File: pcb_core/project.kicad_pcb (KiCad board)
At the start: 2 copper layers, 212.3 x 91.7 mm, 143 parts, among them IC1 DRV8871DDA, IC10 DRV8871DDA, IC11 DRV8871DDA, IC12 DRV8871DDA, IC13 DRV8871DDA, IC14 DRV8871DDA, IC15 DRV8871DDA, IC16 DRV8871DDA, IC17 DRV8871DDA, IC18 DRV8871DDA, IC19 SX1509QBIULTRT, IC2 SX1509QBIULTRT, IC3 DRV8871DDA, IC4 TCA9548APWR, IC5 DRV8871DDA, IC6 DRV8871DDA, IC7 DRV8871DDA, IC8 DRV8871DDA, IC9 DRV8871DDA, J1 Conn_01x02, J10 1053131103, J11 1053131103, J12 1053131103, J13 1053131103, J14 1053131103, J15 1053131103, J16 1053131103, J17 1053131103, J18 1053131103, J19 Conn_02x02_Counter_Clockwise, J2 1725656, J20 PCBConnector, J21 PCBConnector, J22 PCBConnector, J23 PCBConnector, J25 PCBConnector, J27 PCBConnector, J3 1053131103, J4 1053131103, J5 1053131103, J6 1053131103, J7 1053131103, J8 1053131103, J9 1053131103, Q1 SI9945BDY-T1-GE3, U1 ESP32-S3-WROOM-2, U2 LTC4365TS8, U3 ESP32-DevKitC

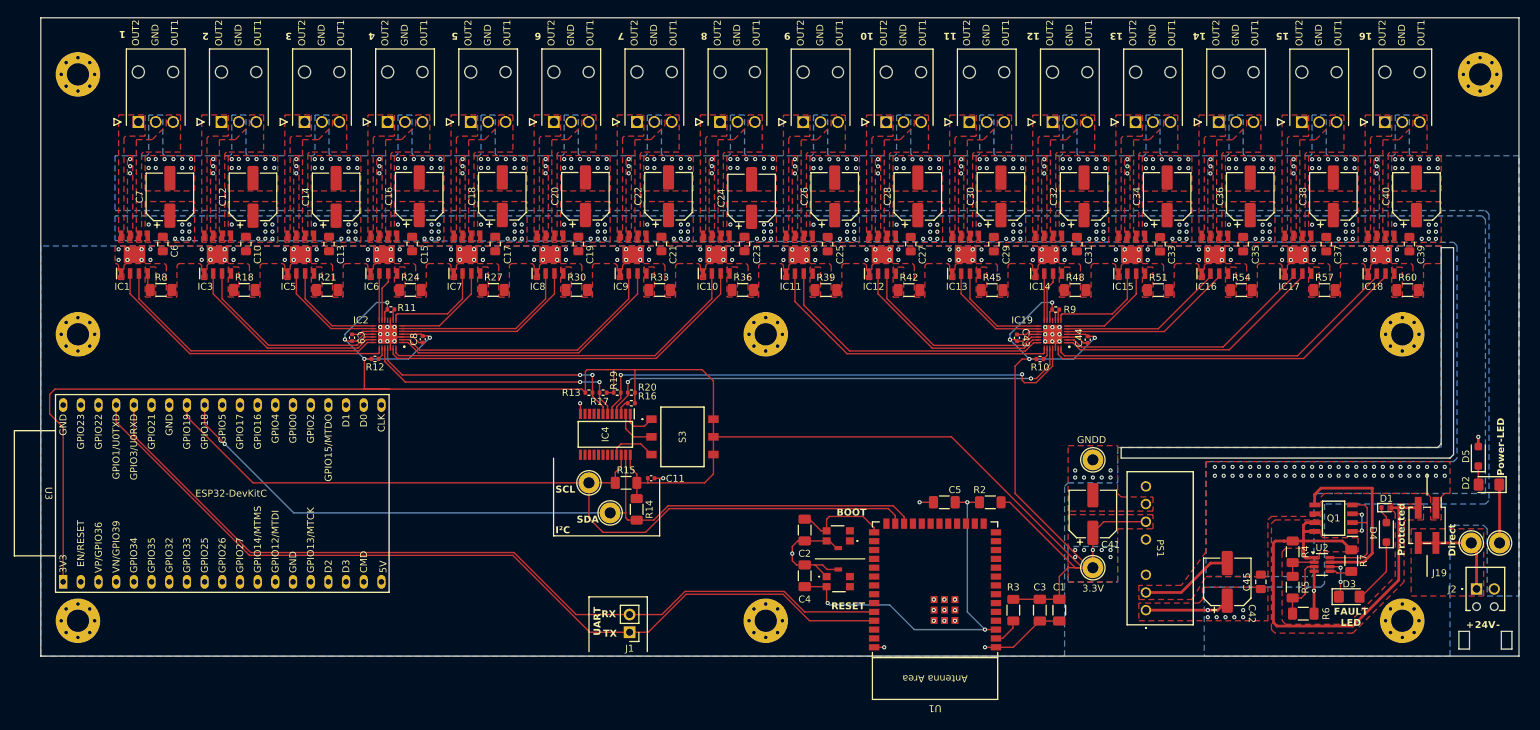
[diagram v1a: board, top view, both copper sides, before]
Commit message: Harmonize package sizing of components
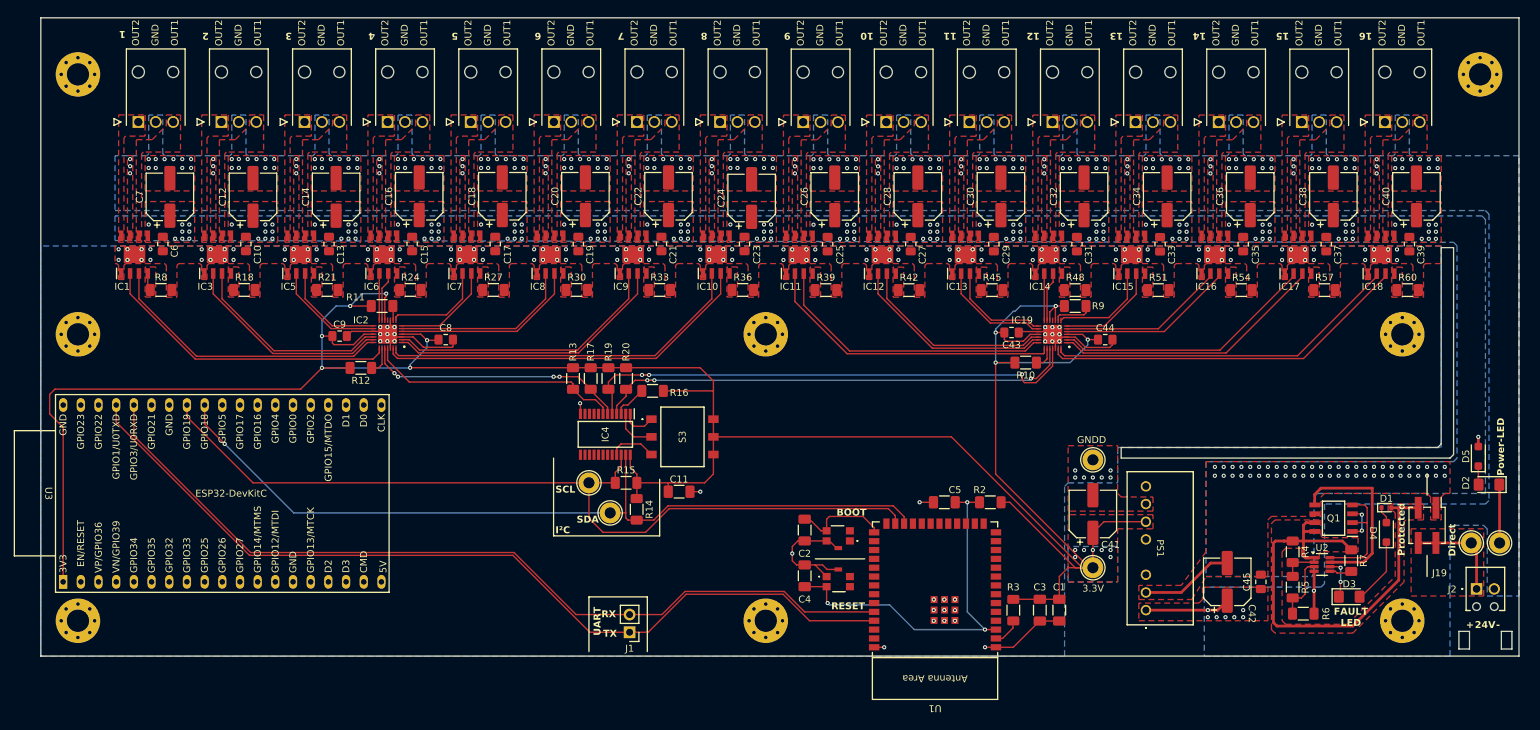
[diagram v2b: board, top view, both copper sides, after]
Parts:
- C11: footprint Capacitor_SMD:C_0402_1005Metric -> Capacitor_SMD:C_1206_3216Metric_Pad1.33x1.80mm_HandSolder
- C43, C44, C8, C9: footprint Capacitor_SMD:C_0402_1005Metric -> Capacitor_SMD:C_0805_2012Metric_Pad1.18x1.45mm_HandSolder
- R10, R11, R12, R13, R16, R17, R19, R20, R9: footprint Resistor_SMD:R_0402_1005Metric -> Resistor_SMD:R_1206_3216Metric_Pad1.30x1.75mm_HandSolder
- moved C11 4.45 mm to (140.0, 109.0)
- moved R16 3.53 mm to (136.1, 94.5)
- moved C8 3.30 mm to (106.4, 87.1), turned to 0 degrees
- moved R13 3.06 mm to (124.7, 92.7), turned to -90 degrees
- moved R9 2.84 mm to (196.8, 82.3)
- moved R17 2.70 mm to (127.3, 92.7), turned to -90 degrees
- moved C44 2.52 mm to (201.2, 87.1), turned to 0 degrees
- moved R12 2.41 mm to (94.2, 91.2)
- moved R19 2.40 mm to (129.8, 92.7), turned to -90 degrees
- moved R20 2.17 mm to (132.3, 92.7), turned to -90 degrees
- moved R10 2.12 mm to (189.7, 90.4)
- moved C9 1.79 mm to (91.2, 86.6), turned to 0 degrees
- moved R11 1.36 mm to (97.3, 82.3)
- moved C43 1.09 mm to (187.7, 86.1), turned to 0 degrees
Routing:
- net VCC_3V3: track 391.6 -> 405.3 mm, vias 15 -> 17
- net GNDD: track 65.7 -> 77.1 mm
- net Net-(IC19-NINT): track 1.63 -> 5.78 mm
- net ~{I2CM_RESET}: track 2.13 -> 4.89 mm
- net Net-(IC2-NRESET): track 1.76 -> 4.05 mm
- net IOEXP01_SCL: track 72.7 -> 74.6 mm, vias 2 -> 3
- net Net-(IC19-NRESET): track 1.76 -> 3.27 mm
- net IOEXP02_SCL: track 38.3 -> 36.9 mm, vias 2 -> 0
- net IN2_2: track 29.7 -> 30.4 mm
- net IN2_1: track 43.0 -> 43.7 mm
- net IN1_1: track 40.9 -> 41.6 mm
- net IN1_2: track 28.7 -> 29.3 mm
- net IOEXP01_SDA: track 69.3 -> 69.8 mm, vias 2 -> 3
- net IOEXP02_SDA: track 39.1 -> 39.4 mm, vias 2 -> 4

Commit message: Update pcb layout
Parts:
- moved C5 17.3 mm to (189.7, 123.2)
- moved R2 16.4 mm to (195.1, 123.2)
- moved R3 7.12 mm to (195.1, 125.7), turned to 180 degrees
- moved C1 4.85 mm to (195.1, 130.8), turned to 180 degrees
- moved C3 4.02 mm to (195.1, 128.3), turned to 180 degrees
- moved D1 0.76 mm to (242.3, 111.3)
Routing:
- net VCC_3V3: track 405.3 -> 367.5 mm
- net /ESP32_EN: track 54.1 -> 42.6 mm, vias 3 -> 2
- net Net-(U1-3V3): track 3.85 -> 9.84 mm
- net GNDA: track 28.9 -> 34.8 mm
- net IOEXP02_SDA: track 39.4 -> 37.9 mm, vias 4 -> 2
- net VIN_24V: track 67.9 -> 66.8 mm
- net IOEXP01_SDA: track 69.8 -> 68.8 mm, vias 3 -> 2
- net IOEXP01_SCL: track 74.6 -> 74.4 mm, vias 3 -> 2
- net PROD_24V: vias 183 -> 156
- net /24V: vias 0 -> 2
- added copper zone on B.Cu, net /24V
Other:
- outline, holes or cut-outs redrawn

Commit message: correct R16 value
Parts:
- R16: value 10K -> 10k
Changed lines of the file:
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@@
 			)
 		)
-		(property "LCSC#" ""
+		(property "LCSC#" "C17902"
 			(at 0 0 180)
 			(unlocked yes)
@@
 			)
 		)
-		(property "LCSC#" ""
+		(property "LCSC#" "C2828875"
 			(at 0 0 -90)
 			(unlocked yes)
@@
 			)
 		)
-		(property "LCSC#" ""
+		(property "LCSC#" "C2828875"
 			(at 0 0 -90)
 			(unlocked yes)
@@
 			)
 		)
+		(property "LCSC#" "C110253"
+			(at 0 0 180)
+			(unlocked yes)
+			(layer "F.Fab")
+			(hide yes)
+			(effects
+				(font
+					(size 1 1)
+					(thickness 0.15)
+				)
+			)
+		)
+		(property "Manufacturer_Part_Number" "Capacitor, 0.1uF, 50V, 10%, 1206 SMD"
+			(at 0 0 180)
+			(unlocked yes)
+			(layer "F.Fab")
+			(hide yes)
+			(effects
+				(font
+					(size 1 1)
+					(thickness 0.15)
+				)
+			)
+		)
 		(property ki_fp_filters "C_*")
 		(sheetname "Stammblatt")
@@
 			)
 		)
+		(property "LCSC#" "C1854361"
+			(at 0 0 180)
+			(unlocked yes)
+			(layer "F.Fab")
+			(hide yes)
+			(effects
+				(font
+					(size 1 1)
+					(thickness 0.15)
+				)
+			)
+		)
 		(property ki_fp_filters "C_*")
 		(sheetname "Stammblatt")
@@
 			)
 		)
+		(property "LCSC#" "C5126164"
+			(at 0 0 0)
+			(unlocked yes)
+			(layer "F.Fab")
+			(hide yes)
+			(effects
+				(font
+					(size 1 1)
+					(thickness 0.15)
+				)
+			)
+		)
 		(property ki_fp_filters "R_*")
 		(sheetname "Stammblatt")
@@
 			)
 		)
+		(property "LCSC#" "C110253"
+			(at 0 0 -90)
+			(unlocked yes)
+			(layer "F.Fab")
+			(hide yes)
+			(effects
+				(font
+					(size 1 1)
+					(thickness 0.15)
+				)
+			)
+		)
+		(property "Manufacturer_Part_Number" "Capacitor, 0.1uF, 50V, 10%, 1206 SMD"
+			(at 0 0 -90)
+			(unlocked yes)
+			(layer "F.Fab")
+			(hide yes)
+			(effects
+				(font
+					(size 1 1)
+					(thickness 0.15)
+				)
+			)
+		)
 		(property ki_fp_filters "C_*")
 		(sheetname "Stammblatt")
@@
 			)
 		)
+		(property "LCSC#" "C17990"
+			(at 0 0 -90)
+			(unlocked yes)
+			(layer "F.Fab")
+			(hide yes)
+			(effects
+				(font
+					(size 1 1)
+					(thickness 0.15)
+				)
+			)
+		)
 		(property ki_fp_filters "R_*")
 		(sheetname "Stammblatt")
@@
 			)
 		)
-		(property "LCSC#" ""
+		(property "LCSC#" "C2828875"
 			(at 0 0 -90)
 			(unlocked yes)
@@
 			)
 		)
-		(property "LCSC#" ""
+		(property "LCSC#" "C17902"
 			(at 0 0 0)
 			(unlocked yes)
@@
 			)
 		)
+		(property "LCSC#" "C2828875"
+			(at 0 0 0)
+			(unlocked yes)
+			(layer "F.Fab")
+			(hide yes)
+			(effects
+				(font
+					(size 1 1)
+					(thickness 0.15)
+				)
+			)
+		)
 		(property ki_fp_filters "R_*")
 		(sheetname "Stammblatt")
@@
 			)
 		)
+		(property "LCSC#" "C14860"
+			(at 0 0 0)
+			(unlocked yes)
+			(layer "F.Fab")
+			(hide yes)
+			(effects
+				(font
+					(size 1 1)
+					(thickness 0.15)
+				)
+			)
+		)
 		(property ki_fp_filters "C_*")
 		(sheetname "Stammblatt")
@@
 			)
 		)
+		(property "LCSC#" "C110253"
+			(at 0 0 90)
+			(unlocked yes)
+			(layer "F.Fab")
+			(hide yes)
+			(effects
+				(font
+					(size 1 1)
+					(thickness 0.15)
+				)
+			)
+		)
+		(property "Manufacturer_Part_Number" "Capacitor, 0.1uF, 50V, 10%, 1206 SMD"
+			(at 0 0 90)
+			(unlocked yes)
+			(layer "F.Fab")
+			(hide yes)
+			(effects
+				(font
+					(size 1 1)
+					(thickness 0.15)
+				)
+			)
+		)
 		(property ki_fp_filters "C_*")
 		(sheetname "Stammblatt")
@@
 			)
 		)
-		(property "Value" "10K"
+		(property "Value" "10k"
 			(at 0 1.82 180)
 			(layer "F.Fab")
@@
 			)
 		)
+		(property "LCSC#" "C17902"
+			(at 0 0 180)
+			(unlocked yes)
+			(layer "F.Fab")
+			(hide yes)
+			(effects
+				(font
+					(size 1 1)
+					(thickness 0.15)
+				)
+			)
+		)
 		(property ki_fp_filters "R_*")
 		(sheetname "Stammblatt")
@@
 			)
 		)
+		(property "LCSC#" "C2828875"
+			(at 0 0 -90)
+			(unlocked yes)
+			(layer "F.Fab")
+			(hide yes)
+			(effects
+				(font
+					(size 1 1)
+					(thickness 0.15)
+				)
+			)
+		)
 		(property ki_fp_filters "R_*")
 		(sheetname "Stammblatt")
@@
 			)
 		)
+		(property "LCSC#" "C17888"
+			(at 0 0 180)
+			(unlocked yes)
+			(layer "F.Fab")
+			(hide yes)
+			(effects
+				(font
+					(size 1 1)
+					(thickness 0.15)
+				)
+			)
+		)
 		(property ki_fp_filters "R_*")
 		(sheetname "Stammblatt")
@@
 			)
 		)
-		(property "LCSC#" ""
+		(property "LCSC#" "C17902"
 			(at 0 0 0)
 			(unlocked yes)
@@
 			)
 		)
-		(property "LCSC#" ""
+		(property "LCSC#" "C17902"
 			(at 0 0 180)
 			(unlocked yes)
@@
 			)
 		)
-		(property "LCSC#" ""
+		(property "LCSC#" "C2828875"
 			(at 0 0 -90)
 			(unlocked yes)
@@
 			)
 		)
+		(property "LCSC#" "C17902"
+			(at 0 0 180)
+			(unlocked yes)
+			(layer "F.Fab")
+			(hide yes)
+			(effects
+				(font
+					(size 1 1)
+					(thickness 0.15)
+				)
+			)
+		)
 		(property ki_fp_filters "R_*")
 		(sheetname "Stammblatt")
@@
 			)
 		)
+		(property "LCSC#" "C14860"
+			(at 0 0 180)
+			(unlocked yes)
+			(layer "F.Fab")
+			(hide yes)
+			(effects
+				(font
+					(size 1 1)
+					(thickness 0.15)
+				)
+			)
+		)
 		(property ki_fp_filters "C_*")
 		(sheetname "Stammblatt")
@@
 			(pts
 				(xy 58.166 72.898) (xy 58.166 68.58) (xy 255.778 68.58) (xy 256.286 69.088) (xy 255.778 110.236)
-				(xy 232.156 110.236) (xy 232.156 121.666) (xy 232.156 121.666) (xy 215.646 121.666) (xy 215.646 132.588)
-				(xy 260.604 132.588) (xy 260.604 123.952) (xy 250.698 123.952) (xy 250.698 114.046) (xy 256.032 114.046)
-				(xy 256.032 123.952) (xy 260.604 123.952) (xy 260.604 123.952) (xy 260.604 40.894) (xy 48.26 40.894)
-				(xy 48.26 72.898)
+				(xy 232.156 110.236) (xy 232.156 121.666) (xy 215.646 121.666) (xy 215.646 132.588) (xy 260.604 132.588)
+				(xy 260.604 123.952) (xy 250.698 123.952) (xy 250.698 114.046) (xy 256.032 114.046) (xy 256.032 123.952)
+				(xy 260.604 123.952) (xy 260.604 40.894) (xy 48.26 40.894) (xy 48.26 72.898)
 			)
 		)

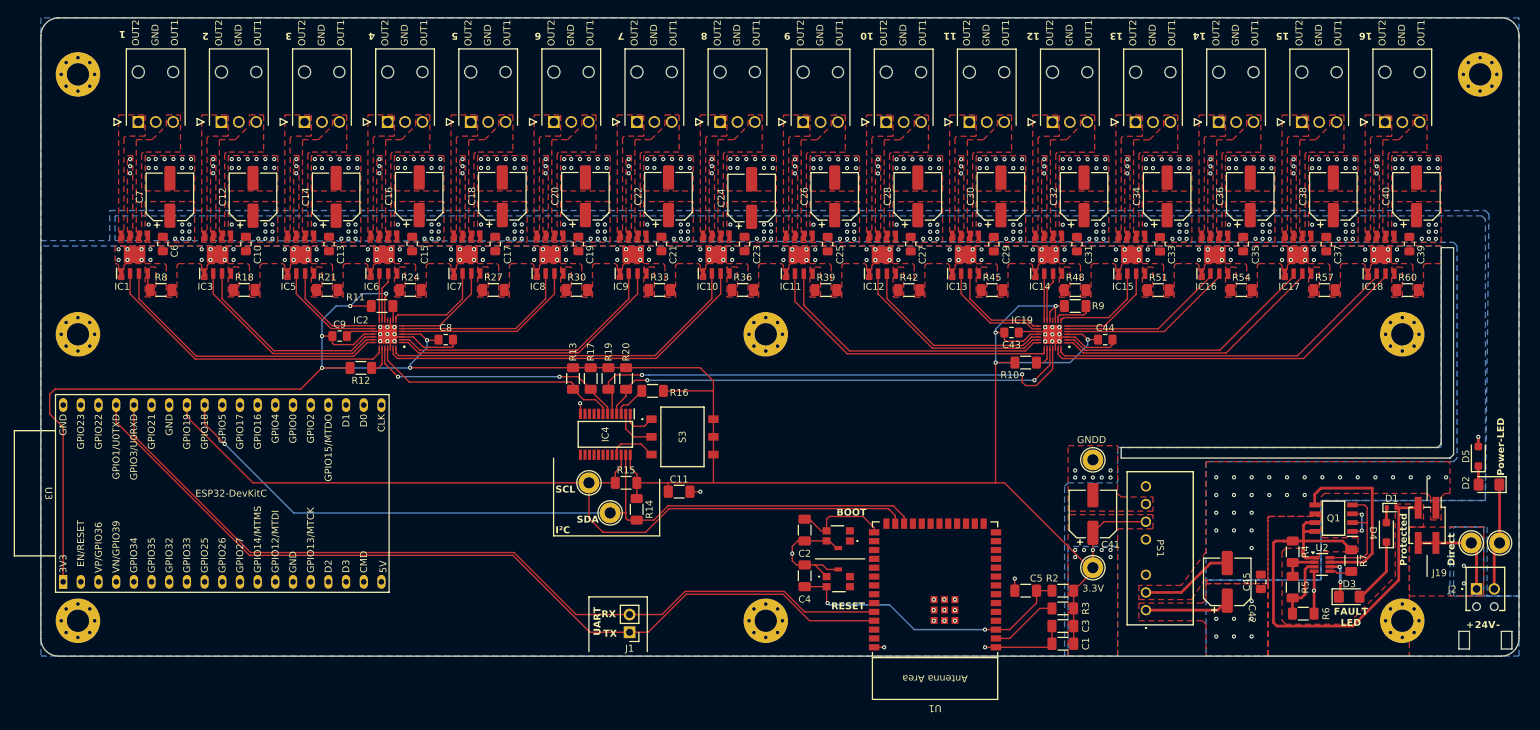
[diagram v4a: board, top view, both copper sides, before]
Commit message: Update pcb, bom and add 3D view
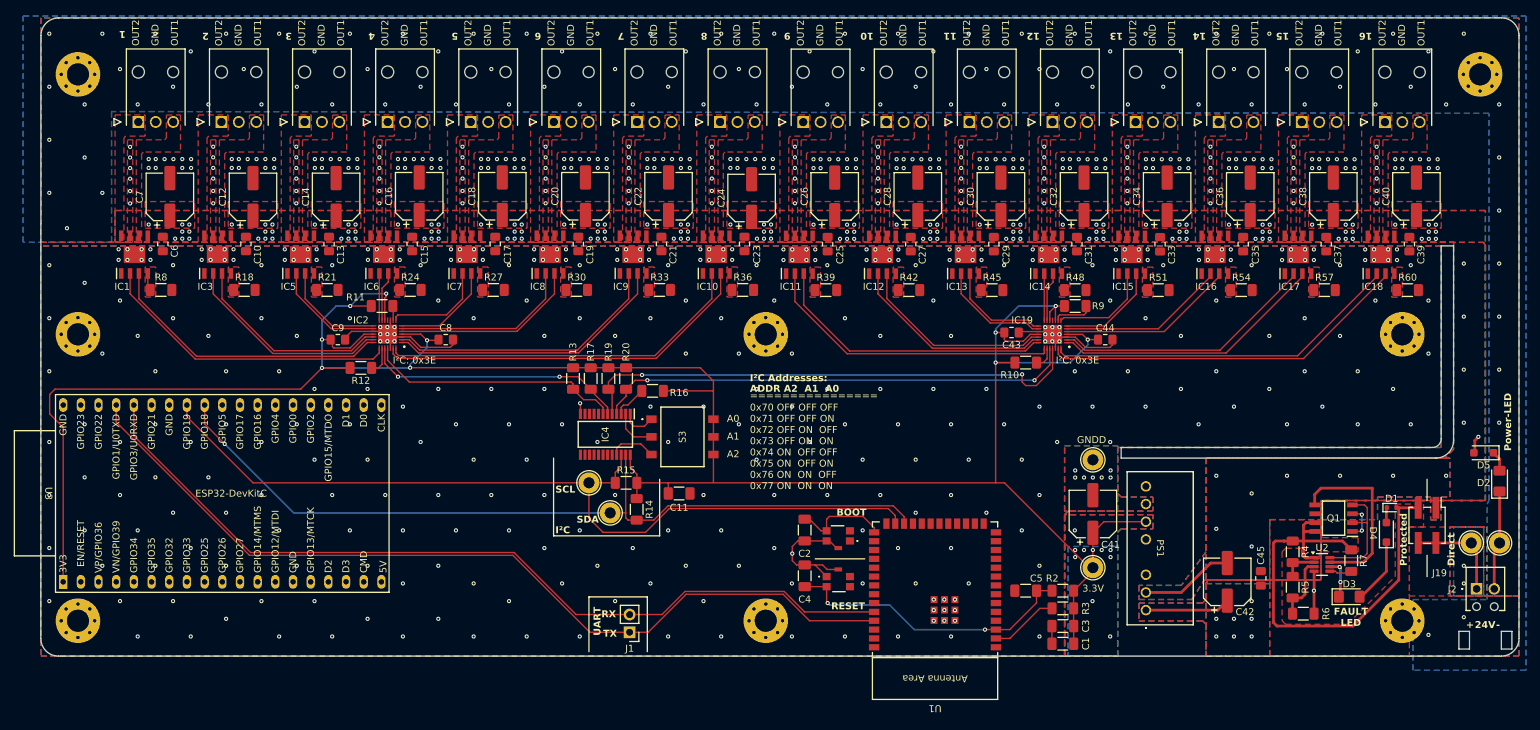
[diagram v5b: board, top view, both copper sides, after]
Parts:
- R4: value 260k -> 250k
- R5: value 40k -> 40.2k
- moved D2 1.61 mm to (257.8, 107.4), turned to 90 degrees
- moved D5 0.92 mm to (255.5, 103.4), turned to 180 degrees
- moved C9 0.57 mm to (90.9, 87.1)
- moved C45 0.51 mm to (223.5, 121.4)
- moved C11 0.25 mm to (140.0, 109.2)
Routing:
- net GNDD: track 77.0 -> 62.8 mm, vias 168 -> 370
- net PROD_24V: track 41.0 -> 42.1 mm, vias 156 -> 141
- net GNDA: track 34.8 -> 33.8 mm, vias 216 -> 359
- net VCC_3V3: vias 17 -> 20
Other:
- outline, holes or cut-outs redrawn
- board text added: "0x70 OFF OFF OFF 0x71 OFF OFF ON 0x72 OFF ON OFF 0x73 OFF ON ON 0x74 ON OFF OFF 0x75 ON OFF ON 0x76 ON ON OFF 0x77 ON ON ON"
- board text added: "================"
- board text added: "A0"
- board text added: "A1"
- board text added: "A2"
- board text added: "ADDR A2 A1 A0"
- board text added: "I²C Addresses:"
- board text added: "I²C: 0x3E"
